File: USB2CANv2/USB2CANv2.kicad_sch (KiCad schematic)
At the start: 64 parts, among them IC1 MIC5528-3.3YMT-TR, J1 USB_C_Receptacle_USB2.0, J2 Conn_01x06_Pin, J3 Conn_01x02_Pin, J4 Conn_01x02_Pin, J5 Conn_01x02_Pin, SW1 SW_BOOT0, U1 STM32F405RGTx, U2 USBLC6-2P6, U3 MCP2561-E-SN, U4 TLP175A, U5 MCP2561-E-SN, U6 TLP175A, Y1 16MHz, Y2 32KHz

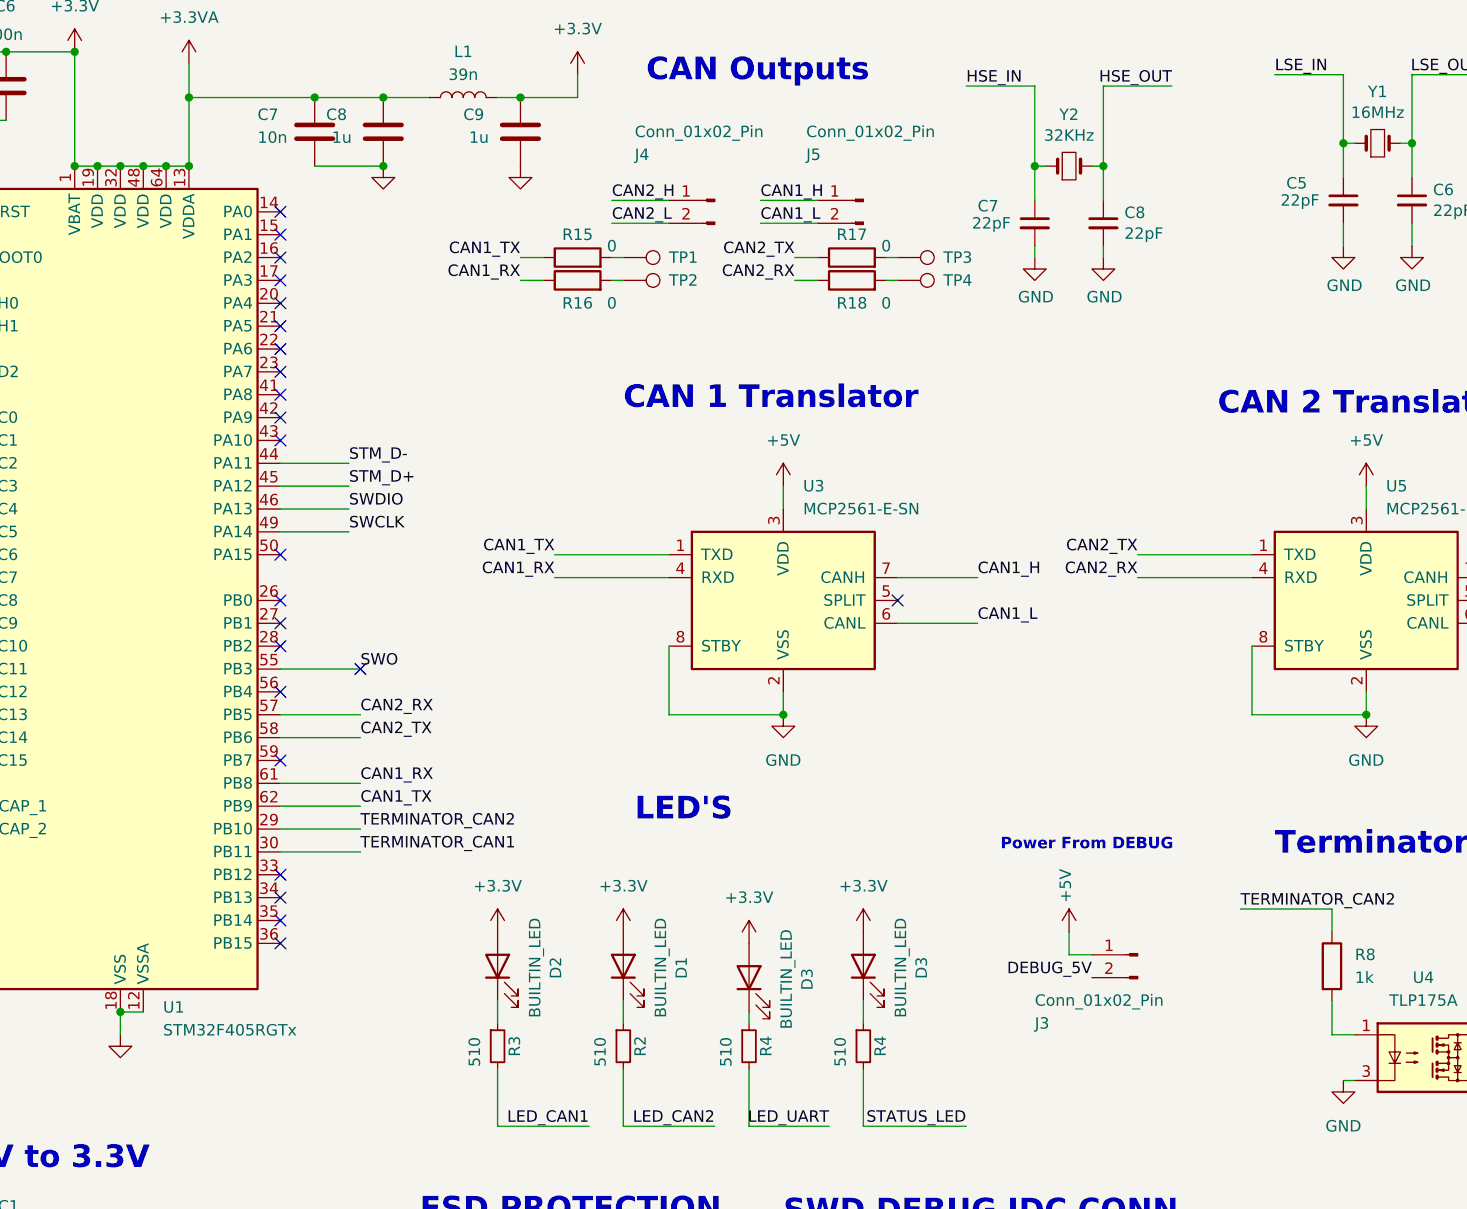
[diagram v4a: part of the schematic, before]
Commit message: Placement done
Placement done, started routing
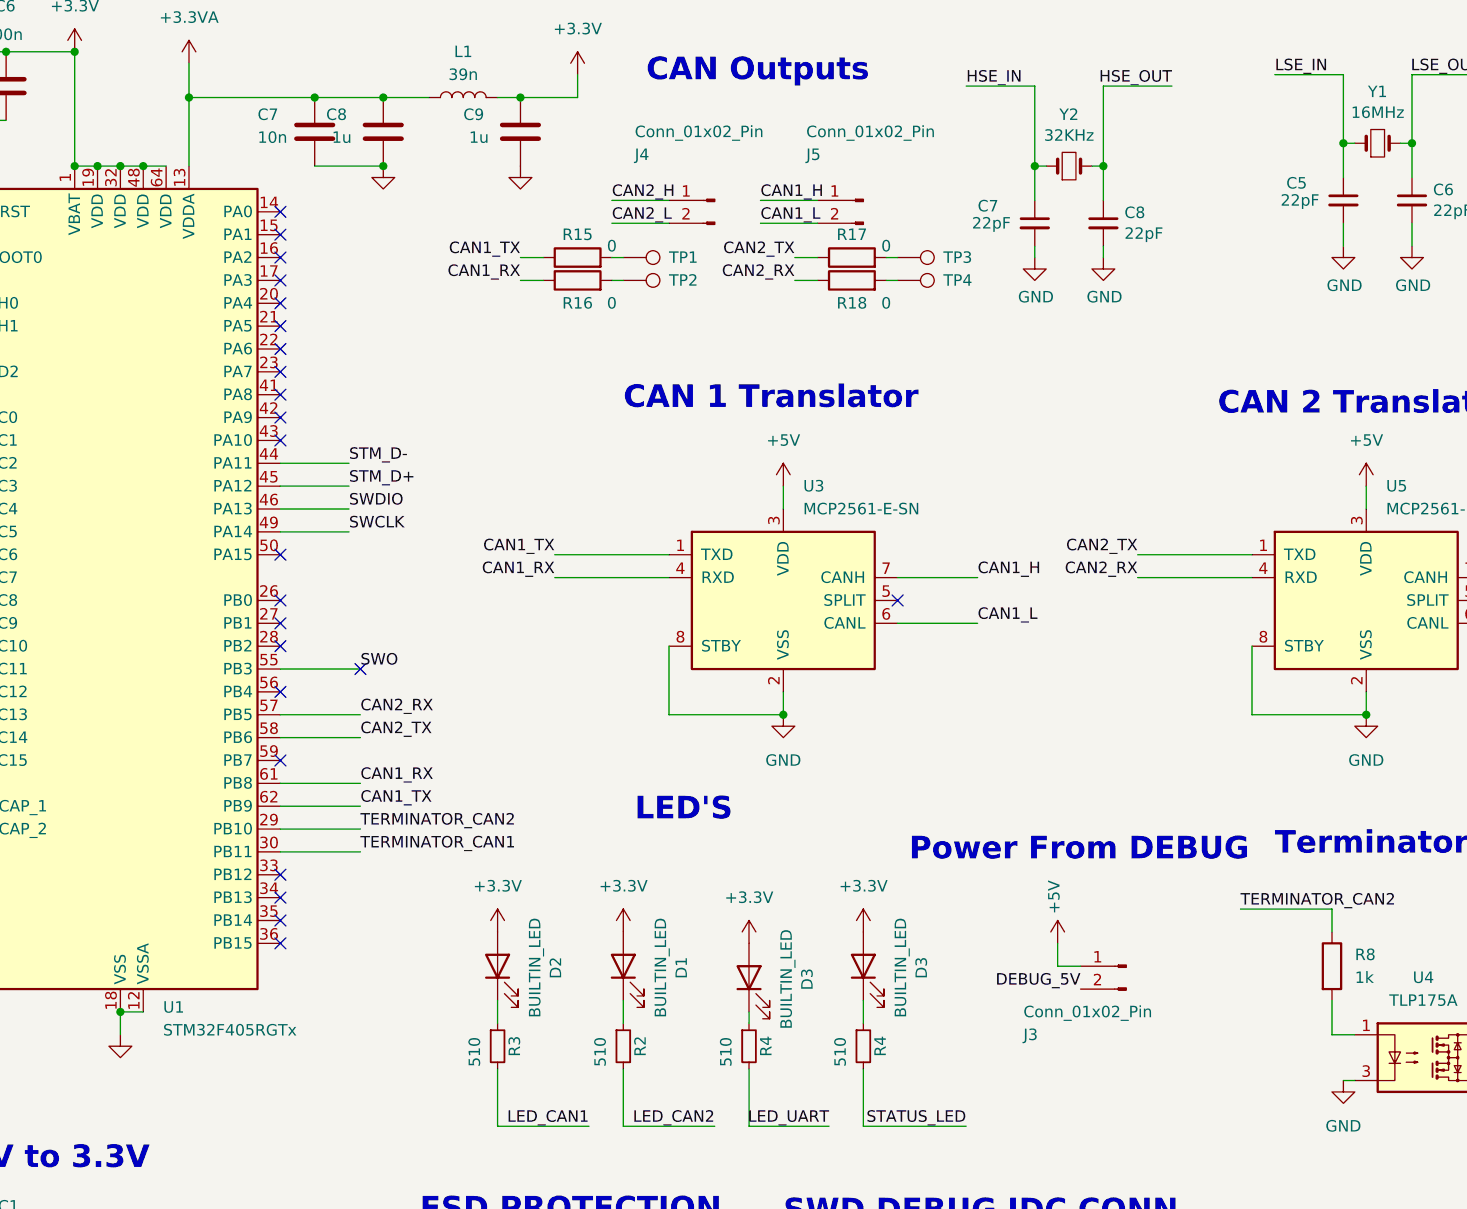
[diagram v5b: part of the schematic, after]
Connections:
- net +3.3V: no longer C7.1, C8.1, L1.1, U1.13 (VDDA)
- new net +3.3VA: C7.1, C8.1, L1.1, U1.13 (VDDA)
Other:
- moved on the sheet: J3
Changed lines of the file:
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@@
     (rev "0.2")
     (company "Gdańsk PGRacingTeam")
-    (comment 1 "Mieszko Celiński")
+    (comment 1 "Karol Pergoł")
+    (comment 2 "Mieszko Celiński")
   )
   (junction (at 92.71 39.37) (diameter 0) (color 0 0 0 0)
@@
   (junction (at 39.37 34.29) (diameter 0) (color 0 0 0 0)
   )
-  (junction (at 71.12 46.99) (diameter 0) (color 0 0 0 0)
-  )
   (junction (at 66.04 46.99) (diameter 0) (color 0 0 0 0)
   )
@@
   )
   (junction (at 207.01 44.45) (diameter 0) (color 0 0 0 0)
-  )
-  (junction (at 68.58 46.99) (diameter 0) (color 0 0 0 0)
   )
   (junction (at 201.93 107.95) (diameter 0) (color 0 0 0 0)
@@
     (stroke (width 0) (type default))
   )
-  (wire (pts (xy 171.45 134.62) (xy 168.91 134.62))
+  (wire (pts (xy 170.18 135.89) (xy 167.64 135.89))
     (stroke (width 0) (type default))
   )
@@
     (stroke (width 0) (type default))
   )
-  (wire (pts (xy 168.91 134.62) (xy 168.91 132.08))
+  (wire (pts (xy 167.64 135.89) (xy 167.64 133.35))
     (stroke (width 0) (type default))
   )
@@
   )
   (wire (pts (xy 250.19 50.8) (xy 250.19 46.99))
-    (stroke (width 0) (type default))
-  )
-  (wire (pts (xy 68.58 46.99) (xy 71.12 46.99))
     (stroke (width 0) (type default))
   )
@@
     (effects (font (size 2.5 2.5) (thickness 0.5) bold) (justify left bottom))
   )
-  (text "Power From DEBUG\n" (at 161.29 123.19 0)
-    (effects (font (size 1.27 1.27) (thickness 0.5) bold) (justify left bottom))
+  (text "Power From DEBUG\n" (at 151.13 124.46 0)
+    (effects (font (size 2.5 2.5) (thickness 0.5) bold) (justify left bottom))
   )
   (text "CAN 2 Translator\n" (at 185.42 74.93 0)
@@
     (effects (font (size 1.27 1.27)) (justify left bottom))
   )
-  (label "DEBUG_5V" (at 171.45 137.16 180) (fields_autoplaced)
+  (label "DEBUG_5V" (at 170.18 138.43 180) (fields_autoplaced)
     (effects (font (size 1.27 1.27)) (justify right bottom))
   )
@@
     )
   )
-  (symbol (lib_id "Connector:Conn_01x02_Pin") (at 176.53 134.62 0) (mirror y) (unit 1)
-    (in_bom yes) (on_board yes) (dnp no)
-    (property "Reference" "J3" (at 165.1 142.24 0)
+  (symbol (lib_id "Connector:Conn_01x02_Pin") (at 175.26 135.89 0) (mirror y) (unit 1)
+    (in_bom yes) (on_board yes) (dnp no)
+    (property "Reference" "J3" (at 163.83 143.51 0)
       (effects (font (size 1.27 1.27)) (justify right))
     )
-    (property "Value" "Conn_01x02_Pin" (at 165.1 139.7 0)
+    (property "Value" "Conn_01x02_Pin" (at 163.83 140.97 0)
       (effects (font (size 1.27 1.27)) (justify right))
     )
-    (property "Footprint" "Connector_PinHeader_2.00mm:PinHeader_1x02_P2.00mm_Vertical" (at 176.53 134.62 0)
-      (effects (font (size 1.27 1.27)) hide)
-    )
-    (property "Datasheet" "~" (at 176.53 134.62 0)
+    (property "Footprint" "Connector_PinHeader_2.00mm:PinHeader_1x02_P2.00mm_Vertical" (at 175.26 135.89 0)
+      (effects (font (size 1.27 1.27)) hide)
+    )
+    (property "Datasheet" "~" (at 175.26 135.89 0)
       (effects (font (size 1.27 1.27)) hide)
     )
@@
     )
   )
-  (symbol (lib_id "power:+5V") (at 168.91 132.08 0) (mirror y) (unit 1)
-    (in_bom yes) (on_board yes) (dnp no)
-    (property "Reference" "#PWR012" (at 168.91 135.89 0)
-      (effects (font (size 1.27 1.27)) hide)
-    )
-    (property "Value" "+5V" (at 168.529 128.8288 90)
-      (effects (font (size 1.27 1.27)) (justify left))
-    )
-    (property "Footprint" "" (at 168.91 132.08 0)
-      (effects (font (size 1.27 1.27)) hide)
-    )
-    (property "Datasheet" "" (at 168.91 132.08 0)
-      (effects (font (size 1.27 1.27)) hide)
-    )
+  (symbol (lib_id "power:+5V") (at 167.64 133.35 0) (mirror y) (unit 1)
+    (in_bom yes) (on_board yes) (dnp no)
+    (property "Reference" "#PWR012" (at 167.64 137.16 0)
+      (effects (font (size 1.27 1.27)) hide)
+    )
+    (property "Value" "+5V" (at 167.259 130.0988 90)
+      (effects (font (size 1.27 1.27)) (justify left))
+    )
+    (property "Footprint" "" (at 167.64 133.35 0)
+      (effects (font (size 1.27 1.27)) hide)
+    )
+    (property "Datasheet" "" (at 167.64 133.35 0)
+      (effects (font (size 1.27 1.27)) hide)
+    )

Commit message: board routed
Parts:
- SW1: footprint Button_Switch_SMD:SW_SPDT_PCM12 -> Jumper:SolderJumper-3_P1.3mm_Open_RoundedPad1.0x1.5mm_NumberLabels
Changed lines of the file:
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@@
     )
   )
-  (symbol (lib_id "Device:C") (at 20.32 38.1 0) (unit 1)
-    (in_bom yes) (on_board yes) (dnp no)
-    (property "Reference" "C1" (at 19.05 29.21 0)
-      (effects (font (size 1.27 1.27)) (justify left))
-    )
-    (property "Value" "10u" (at 18.415 32.385 0)
-      (effects (font (size 1.27 1.27)) (justify left))
-    )
-    (property "Footprint" "Capacitor_SMD:C_0402_1005Metric_Pad0.74x0.62mm_HandSolder" (at 21.2852 41.91 0)
+  (symbol (lib_id "Device:C") (at 20.32 38.1 0) (mirror y) (unit 1)
+    (in_bom yes) (on_board yes) (dnp no)
+    (property "Reference" "C1" (at 21.59 29.21 0)
+      (effects (font (size 1.27 1.27)) (justify left))
+    )
+    (property "Value" "10u" (at 22.225 32.385 0)
+      (effects (font (size 1.27 1.27)) (justify left))
+    )
+    (property "Footprint" "Capacitor_SMD:C_0402_1005Metric_Pad0.74x0.62mm_HandSolder" (at 19.3548 41.91 0)
       (effects (font (size 1.27 1.27)) hide)
     )
@@
       (effects (font (size 1.27 1.27)))
     )
-    (property "Footprint" "Button_Switch_SMD:SW_SPDT_PCM12" (at 29.21 57.15 0)
-      (effects (font (size 1.27 1.27)) hide)
-    )
+    (property "Footprint" "Jumper:SolderJumper-3_P1.3mm_Open_RoundedPad1.0x1.5mm_NumberLabels" (at 29.21 57.15 0)
+      (effects (font (size 1.27 1.27)) hide)
+    )

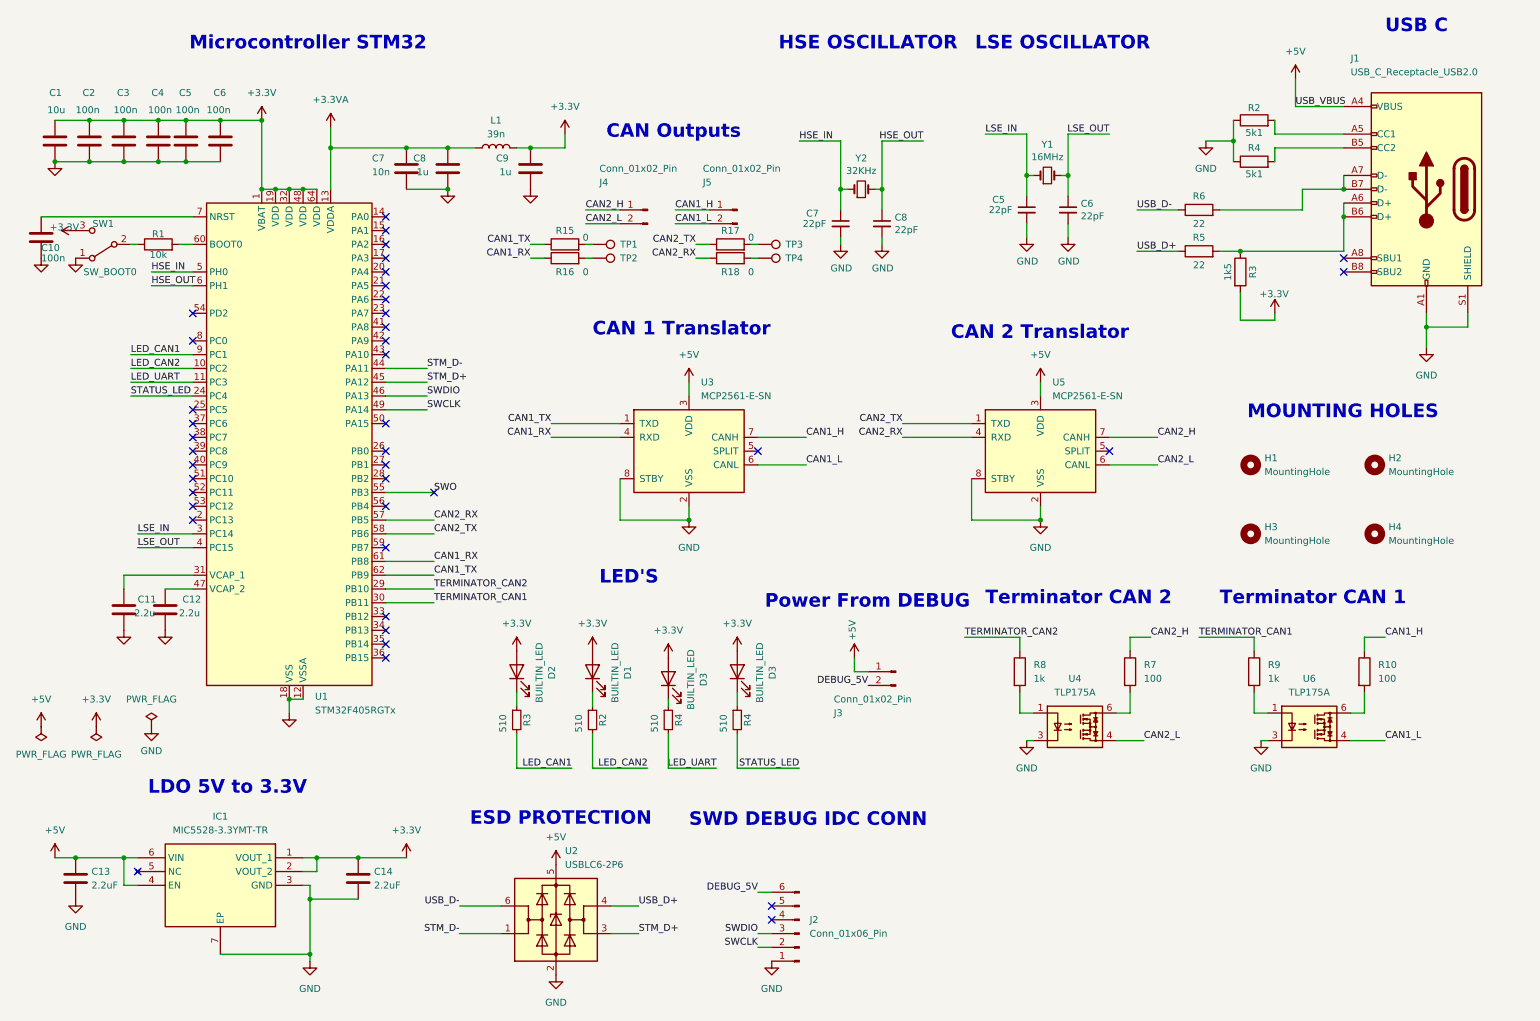
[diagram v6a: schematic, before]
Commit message: Changed stack-up, Silkscreen improvments + LSE HSE SWAP
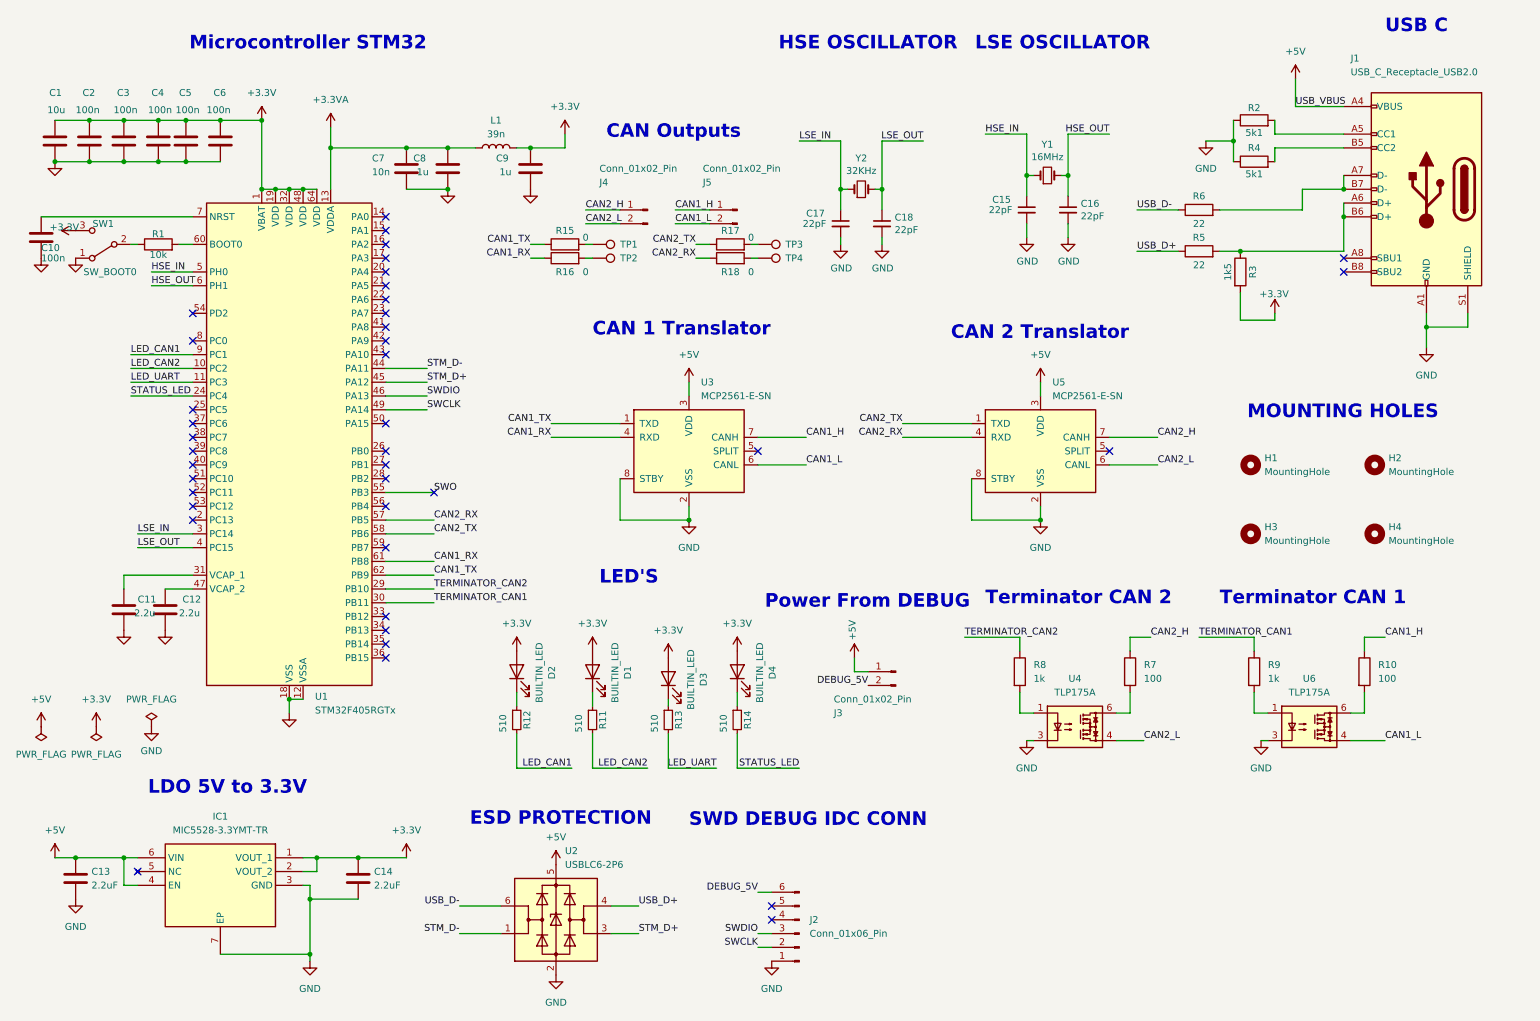
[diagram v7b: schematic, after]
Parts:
- renumbered C5 to C15, C6 to C16, C7 to C17, C8 to C18, D3 to D4, R2 to R11, R3 to R12, R4 to R13, R4 to R14
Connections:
- net HSE_IN: now also C15.1, Y1.1; no longer C17.1, Y2.1
- net HSE_OUT: now also C16.1, Y1.2; no longer C18.1, Y2.2
- net LSE_IN: now also C17.1, Y2.1; no longer C15.1, Y1.1
- net LSE_OUT: now also C18.1, Y2.2; no longer C16.1, Y1.2

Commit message: schematic revision updated
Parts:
- J3: footprint Connector_PinHeader_2.00mm:PinHeader_1x02_P2.00mm_Vertical -> Connector_PinHeader_2.54mm:PinHeader_1x02_P2.54mm_Vertical
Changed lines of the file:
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@@
 		(title "USB2CAN- CAN TO UART TRANSLATION")
 		(date "2024-01-10")
-		(rev "0.2")
+		(rev "0.3")
 		(company "Gdańsk PGRacingTeam")
-		(comment 1 "Karol Pergoł")
-		(comment 2 "Mieszko Celiński")
+		(comment 1 "Mieszko Celiński")
 	)
 	(text "Microcontroller STM32 \n"
@@
 			)
 		)
-		(property "Footprint" "Connector_PinHeader_2.00mm:PinHeader_1x02_P2.00mm_Vertical"
+		(property "Footprint" "Connector_PinHeader_2.54mm:PinHeader_1x02_P2.54mm_Vertical"
 			(at 175.26 135.89 0)
 			(effects
